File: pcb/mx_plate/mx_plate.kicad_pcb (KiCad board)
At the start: 2 copper layers, 134.8 x 111.5 mm, 34 parts, among them SW1 SW_PUSH, SW10 SW_PUSH, SW11 SW_PUSH, SW12 SW_PUSH, SW13 SW_PUSH, SW14 SW_PUSH, SW15 SW_PUSH, SW16 SW_PUSH, SW17 SW_PUSH, SW18 SW_PUSH, SW19 SW_PUSH, SW2 SW_PUSH, SW20 SW_PUSH, SW21 SW_PUSH, SW22 SW_PUSH, SW23 SW_PUSH, SW24 SW_PUSH, SW25 SW_PUSH, SW26 SW_PUSH, SW27 SW_PUSH, SW28 SW_PUSH, SW29 SW_PUSH, SW3 SW_PUSH, SW30 SW_PUSH, SW4 SW_PUSH, SW5 SW_PUSH, SW6 SW_PUSH, SW7 SW_PUSH, SW8 SW_PUSH, SW9 SW_PUSH

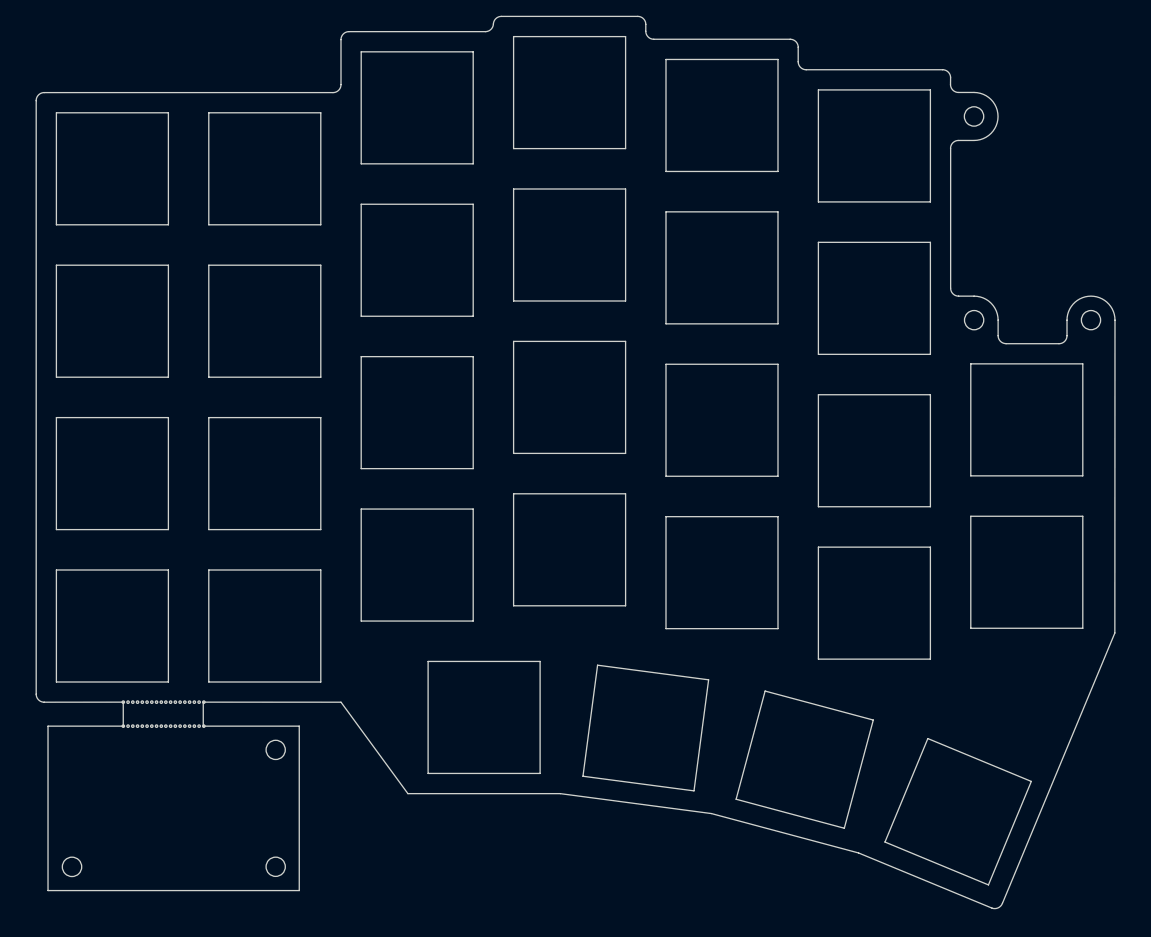
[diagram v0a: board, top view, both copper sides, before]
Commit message: feat: sage60 case generator, phi6 magnets and shared plate
- mechanical/case: scripts that build the split case (MX and low-profile) in Fusion from KiCad
  (outline, gasket shelf, USB-C, slide switch, MCU cover, trackball), with interference checks and
  PCB/switch/keycap reference models for renders
- top case: case A (skirt down to the desk); guards over the gaps between the main block, the thumb
  cluster and the right column; the bare PCB around the trackball is covered too
- magnets: Daiso phi6x3, 4 per side
- left PCB: reroute ROW4 near SW28 and add a semicircular edge notch for a magnet post
- plate: one plate for both halves; the right half snips off the trackball part (slots + bridges)
  and the front gasket tab (mouse bites) and is used flipped

Co-Authored-By: Claude Opus 5.5 <noreply@anthropic.com>
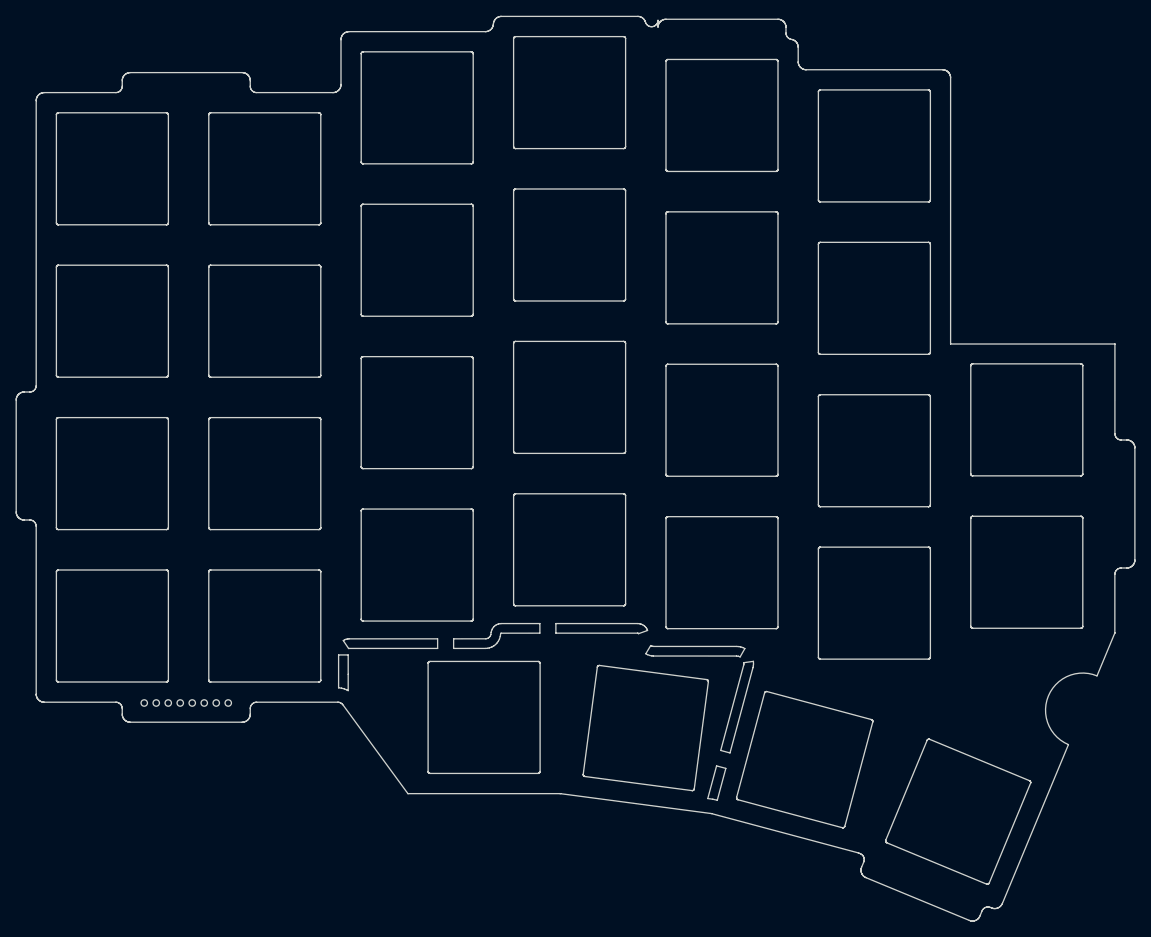
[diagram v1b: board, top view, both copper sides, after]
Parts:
- removed REF** (x4): Breakaway_Tabs, 0_kbd:Breakaway_Tabs
- removed SW1, SW10, SW11, SW12, SW13, SW14, SW15, SW16, SW17, SW18, SW19, SW2, SW20, SW21, SW22, SW23, SW24, SW25, SW26, SW27, SW28, SW29, SW3, SW30, SW4, SW5, SW6, SW7, SW8, SW9: SW_PUSH, 0_kbd:SW_Hole
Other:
- board size 134.8 x 111.5 mm -> 139.8 x 113.1 mm
- board text added: "SW1"
- board text added: "SW10"
- board text added: "SW11"
- board text added: "SW12"
- board text added: "SW13"
- board text added: "SW14"
- board text added: "SW15"
- board text added: "SW16"
- board text added: "SW17"
- board text added: "SW18"
- board text added: "SW19"
- board text added: "SW2"
- board text added: "SW20"
- board text added: "SW21"
- board text added: "SW22"
- board text added: "SW23"
- board text added: "SW24"
- board text added: "SW25"
- board text added: "SW26"
- board text added: "SW27"
- board text added: "SW28"
- board text added: "SW29"
- board text added: "SW3"
- board text added: "SW30"
- board text added: "SW4"
- board text added: "SW5"
- board text added: "SW6"
- board text added: "SW7"
- board text added: "SW8"
- board text added: "SW9"
